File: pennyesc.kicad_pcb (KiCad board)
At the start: 2 copper layers, 34.5 x 40.2 mm, 52 parts, among them U1 MA782GGU-Z, U2 STM32L011F4Ux, U3 MP6536DU-LF-Z, U5 LM3480-3.3

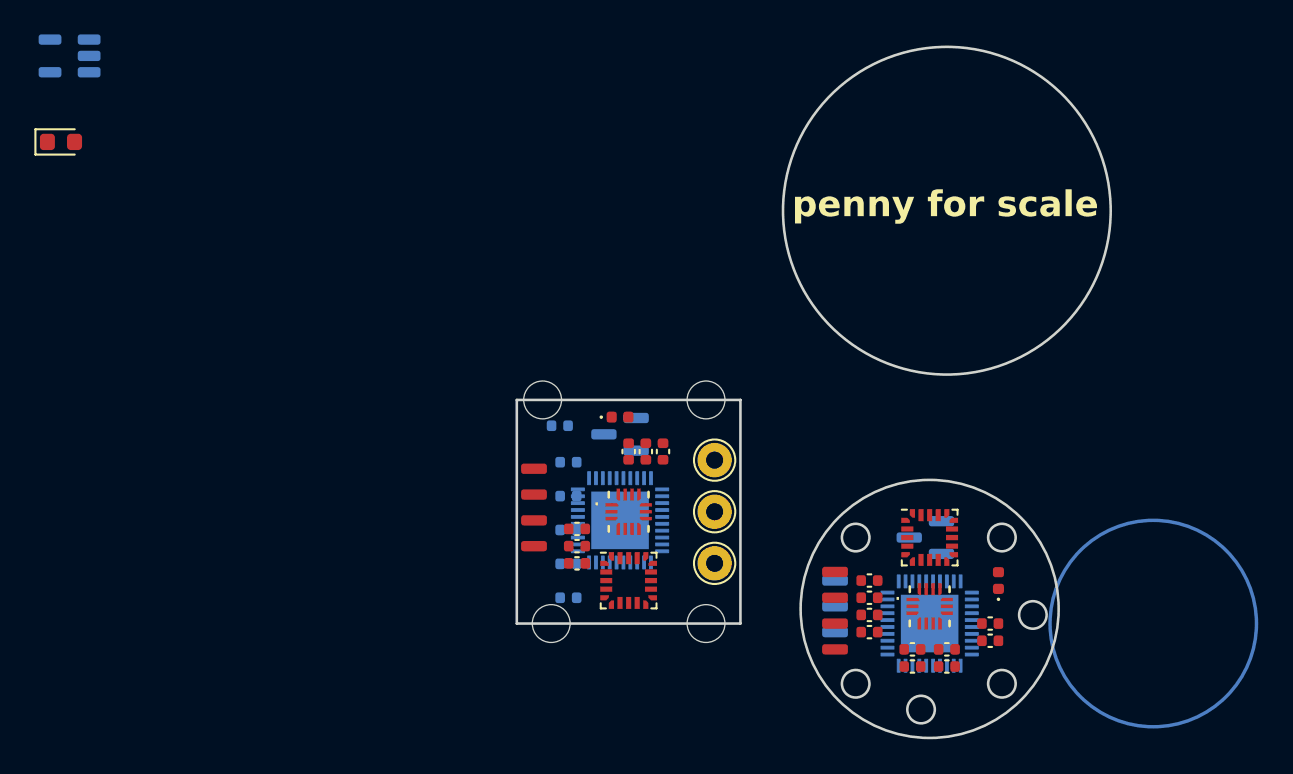
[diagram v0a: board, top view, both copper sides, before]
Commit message: pin assignment with stm32cube, pick LDO
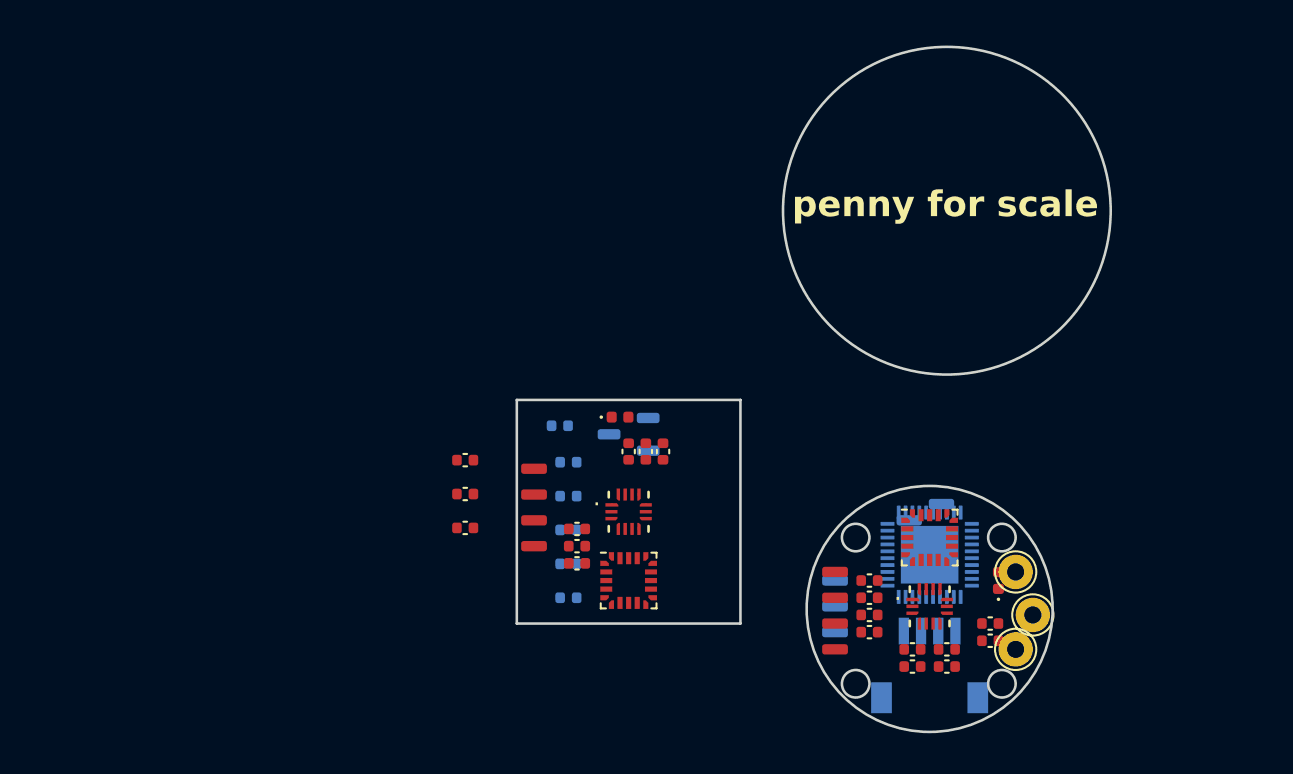
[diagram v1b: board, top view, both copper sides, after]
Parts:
- removed the REF** at (55.0, 47.0)
- removed the REF** at (45.5, 56.5)
- removed the REF** at (17.5, 23.5)
- removed the REF** at (55.0, 50.0)
- removed the REF** at (17.0, 28.5)
- removed the REF** at (55.0, 53.0)
- removed the REF** at (54.5, 56.5)
- removed the REF** at (54.5, 43.5)
- removed the REF** at (45.0, 43.5)
- removed the U3 at (67.5, 56.5)
- removed the U5 at (49.5, 45.5)
- added C10: 1uF, Capacitor_SMD:C_0402_1005Metric, F.Cu at (40.5, 50.9)
- added C7: 1uF, Capacitor_SMD:C_0402_1005Metric, F.Cu at (40.5, 47.0)
- added C9: 1uF, Capacitor_SMD:C_0402_1005Metric, F.Cu at (40.5, 49.0)
- added REF**: TestPoint_THTPad_D2.0mm_Drill1.0mm, TestPoint:TestPoint_THTPad_D2.0mm_Drill1.0mm, F.Cu at (73.5, 56.0)
- added REF**: JST_SM04B-SRSS-TB_LF__SN_, pennyesc:JST_SM04B-SRSS-TB(LF)(SN), B.Cu at (67.5, 56.9)
- added REF**: TestPoint_THTPad_D2.0mm_Drill1.0mm, TestPoint:TestPoint_THTPad_D2.0mm_Drill1.0mm, F.Cu at (72.5, 53.5)
- added REF**: TestPoint_THTPad_D2.0mm_Drill1.0mm, TestPoint:TestPoint_THTPad_D2.0mm_Drill1.0mm, F.Cu at (72.5, 58.0)
- added U6: XC6206P332MR-G, Package_TO_SOT_SMD:SOT-23-3, B.Cu at (50.0, 45.5)
- moved U3 18.1 mm to (67.5, 52.5)
- moved U5 1.00 mm to (67.2, 50.5)
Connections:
- net Net-(U5-VI) renamed VBUS
- U1 pad 1: unconnected-(U1-SCLK-Pad1) -> /SPI_SCLK
- U1 pad 11: unconnected-(U1-EN-Pad11) -> +3.3V
- U1 pad 5: unconnected-(U1-MISO-Pad5) -> /SPI_MISO
- U1 pad 6: unconnected-(U1-ASC-Pad6) -> GND
- U1 pad 8: unconnected-(U1-MOSI-Pad8) -> /SPI_MOSI
- U2 pad 10: unconnected-(U2-PA7-Pad10) -> /SPI_MOSI
- U2 pad 14: unconnected-(U2-PA9-Pad14) -> /UART_TX
- U2 pad 15: unconnected-(U2-PA10-Pad15) -> /UART_RX
- U2 pad 16: unconnected-(U2-PA13-Pad16) -> /SWDIO
- U2 pad 17: unconnected-(U2-PA14-Pad17) -> /SWCLK
- U2 pad 20: unconnected-(U2-PB9-Pad20) -> GND
- U2 pad 3: unconnected-(U2-NRST-Pad3) -> /NRST
- U2 pad 6: unconnected-(U2-PA1-Pad6) -> /UART_DE
- U2 pad 8: unconnected-(U2-PA5-Pad8) -> /SPI_SCLK
- U2 pad 9: unconnected-(U2-PA6-Pad9) -> /SPI_MISO
- U3 pad 12: unconnected-(U3-PWM1-Pad12) -> /PWM1
- U3 pad 13: unconnected-(U3-PWM2-Pad13) -> /PWM2
- U3 pad 15: unconnected-(U3-SHDNB-Pad15) -> +3.3V
- U3 pad 16: unconnected-(U3-PWM3-Pad16) -> /PWM3
- U3 pad 17: unconnected-(U3-STBYB-Pad17) -> /STBY
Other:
- board size 34.5 x 40.2 mm -> 34.5 x 39.8 mm

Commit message: switch to cheaper TI parts, passthrough shaft
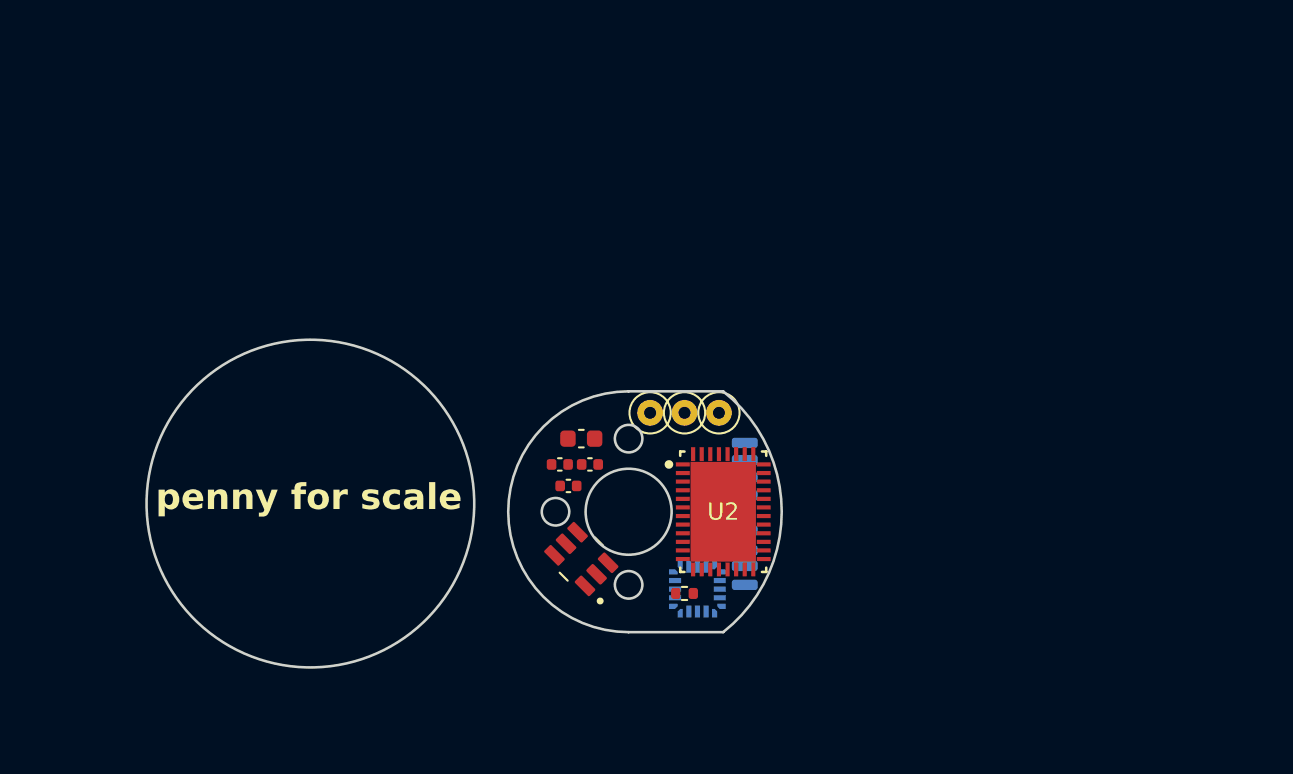
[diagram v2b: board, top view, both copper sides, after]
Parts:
- removed the C2 at (66.5, 58.0)
- removed the C2 at (71.0, 57.5)
- removed the C2 at (68.5, 58.0)
- removed the C2 at (64.0, 57.0)
- removed the C2 at (64.0, 56.0)
- removed the C2 at (68.5, 59.0)
- removed the C2 at (66.5, 59.0)
- removed the C2 at (47.0, 53.0)
- removed the C2 at (46.5, 47.1)
- removed the C2 at (50.0, 46.5)
- removed the C2 at (52.0, 46.5)
- removed the C2 at (64.0, 55.0)
- removed the C2 at (51.0, 46.5)
- removed the C2 at (64.0, 54.0)
- removed the C2 at (71.0, 56.5)
- removed the C2 at (47.0, 51.0)
- removed the C2 at (47.0, 52.0)
- removed C4: 0.1uF, Capacitor_SMD:C_0402_1005Metric
- removed the REF** at (49.5, 44.5)
- removed the REF** at (44.5, 47.5)
- removed the REF** at (62.0, 53.5)
- removed the REF** at (73.5, 56.0)
- removed the REF** at (44.5, 49.0)
- removed the REF** at (67.5, 56.9)
- removed the REF** at (62.0, 54.0)
- removed the REF** at (62.0, 57.0)
- removed the REF** at (62.0, 55.5)
- removed the REF** at (72.5, 58.0)
- removed the REF** at (62.0, 55.0)
- removed the REF** at (62.0, 56.5)
- removed the REF** at (62.0, 58.0)
- removed the REF** at (44.5, 52.0)
- removed the REF** at (44.5, 50.5)
- removed the REF** at (71.5, 54.0)
- removed the U1 at (50.0, 50.0)
- removed the U1 at (67.5, 55.5)
- removed the U2 at (67.5, 51.5)
- removed the U2 at (50.0, 54.0)
- removed U5: LM3480-3.3, Package_TO_SOT_SMD:SOT-23
- removed U6: XC6206P332MR-G, Package_TO_SOT_SMD:SOT-23-3
- added R1: 22R, Resistor_SMD:R_0402_1005Metric, F.Cu at (53.2, 54.8)
- added REF**: TestPoint_THTPad_D2.0mm_Drill1.0mm, TestPoint:TestPoint_THTPad_D2.0mm_Drill1.0mm, F.Cu at (53.2, 44.2)
- added REF**: TestPoint_THTPad_D2.0mm_Drill1.0mm, TestPoint:TestPoint_THTPad_D2.0mm_Drill1.0mm, F.Cu at (51.2, 44.2)
- added TP1: TestPoint, pennyesc:TestPoint_Pad_Rect, B.Cu at (56.8, 48.0)
- added TP2: TestPoint, pennyesc:TestPoint_Pad_Rect, B.Cu at (56.8, 46.0)
- added TP3: TestPoint, pennyesc:TestPoint_Pad_Rect, B.Cu at (56.8, 47.0)
- added TP4: TestPoint, pennyesc:TestPoint_Pad_Rect, B.Cu at (56.8, 49.0)
- added TP5: TestPoint, pennyesc:TestPoint_Pad_Rect, B.Cu at (56.8, 51.1)
- added TP6: TestPoint, pennyesc:TestPoint_Pad_Rect, B.Cu at (56.8, 53.1)
- added TP7: TestPoint, pennyesc:TestPoint_Pad_Rect, B.Cu at (56.8, 54.2)
- added TP8: TestPoint, pennyesc:TestPoint_Pad_Rect, B.Cu at (56.8, 52.2)
- added U1: STM32L011F4Ux, Package_DFN_QFN:ST_UFQFPN-20_3x3mm_P0.5mm, B.Cu at (54.0, 54.5)
- added U2: MCT8316Z0RRGFR, pennyesc:MCT8316Z0RRGFR-IPC_C, F.Cu at (55.5, 50.0)
- C3: value 0.1uF -> 22uF; footprint Capacitor_SMD:C_0402_1005Metric -> Capacitor_SMD:C_0603_1608Metric; moved to F.Cu
- U3: value MP6536DU-LF-Z -> TMAG5273A1QDBVR; footprint pennyesc:QFN40P500X500X100-41N_MP6536DU-LF-Z -> pennyesc:SOT95P280X140-6N; moved to F.Cu
- moved U3 20.3 mm to (47.2, 52.8), turned to 135 degrees
- moved REF** 19.6 mm to (55.2, 44.2)
- moved C1 9.50 mm to (54.5, 49.2)
- moved C5 9.45 mm to (54.5, 48.0)
- moved C6 9.18 mm to (54.5, 50.5)
- moved C7 7.25 mm to (47.8, 47.2)
- moved C1 6.48 mm to (46.5, 48.5)
- moved C2 5.76 mm to (46.0, 47.2)
- moved C3 3.42 mm to (47.2, 45.8), turned to 0 degrees
- renumbered C10 to C1, C9 to C2
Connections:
- C3 pad 1: Net-(U3-BST2) -> GND
- C3 pad 2: Net-(C3-Pad2) -> Net-(U2-FB_BK)
- U3 pad 1: Net-(C3-Pad2) -> /I2C_SCL
- U3 pad 2: Net-(C3-Pad2) -> GND
- U3 pad 3: VBUS -> GND
- U3 pad 4: VBUS -> +3.3V
- U3 pad 5: VBUS -> unconnected-(U3-~{INT}-Pad5)
- U3 pad 6: Net-(C4-Pad2) -> /I2C_SDA
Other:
- board size 34.5 x 39.8 mm -> 36.9 x 19 mm

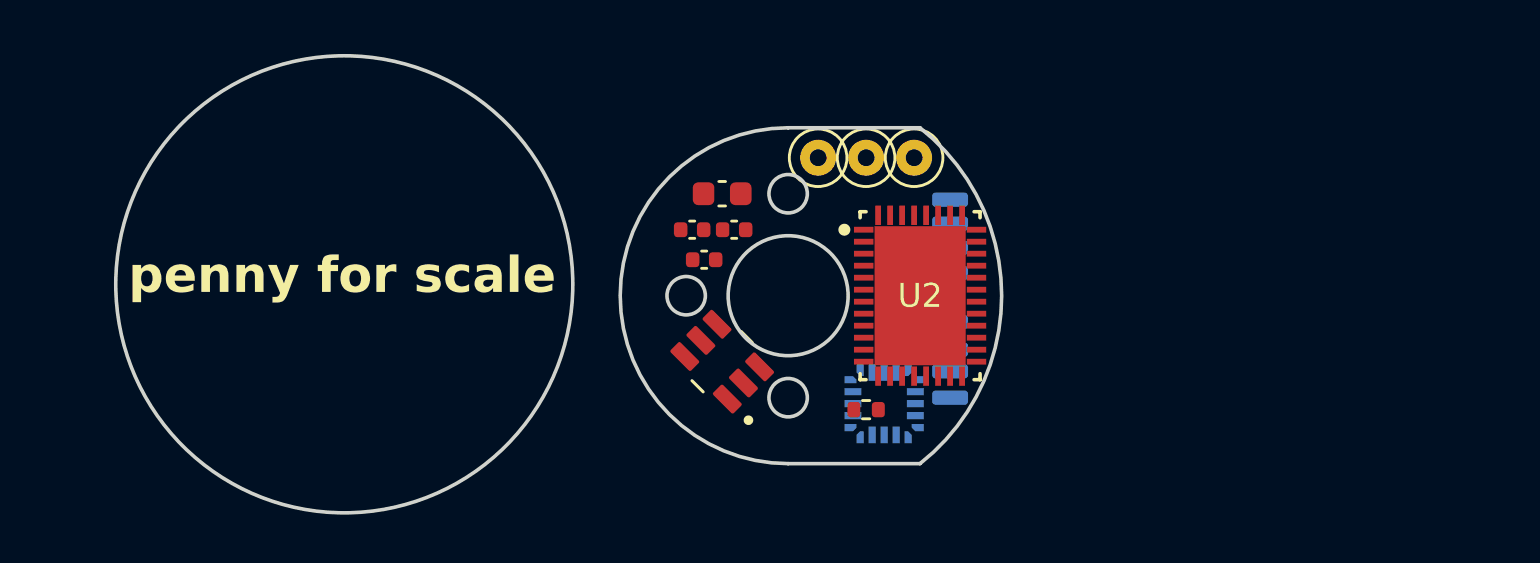
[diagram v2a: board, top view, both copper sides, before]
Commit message: chose R and C values, set jlcpcb constraints, started layout
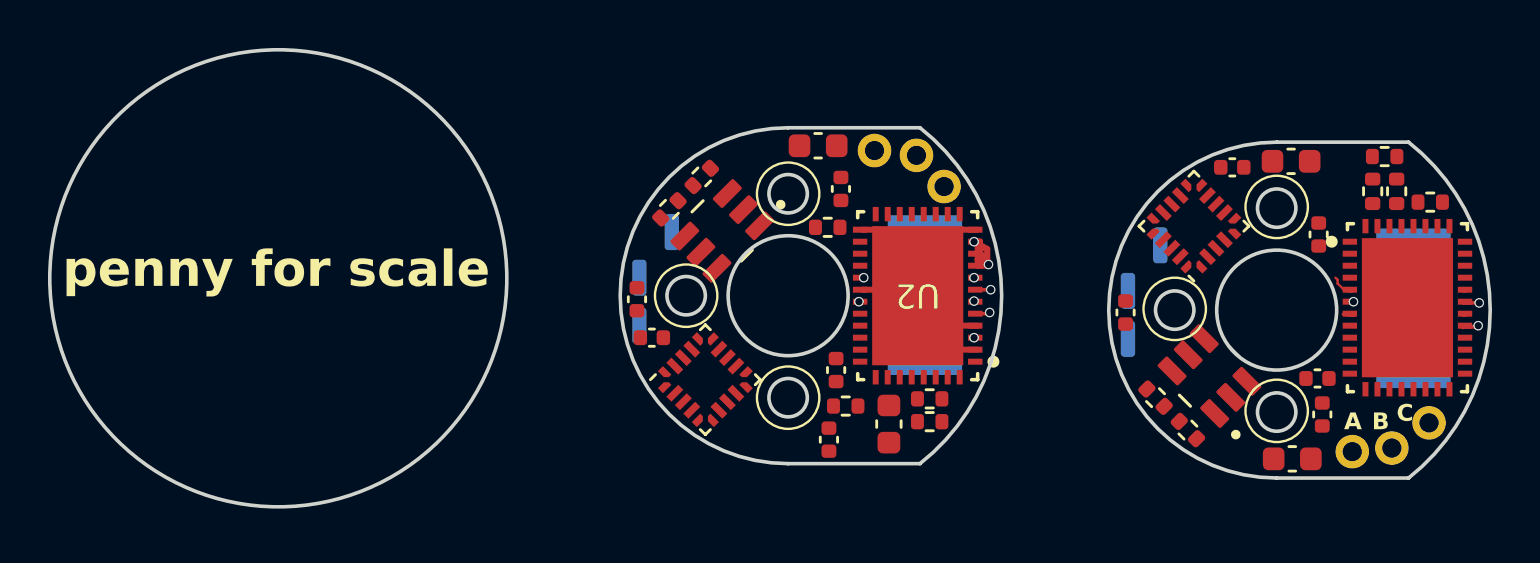
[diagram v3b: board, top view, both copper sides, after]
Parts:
- removed the C5 at (54.5, 48.0)
- removed the C6 at (54.5, 50.5)
- removed the C7 at (47.8, 47.2)
- removed REF** (x3): TestPoint_THTPad_D2.0mm_Drill1.0mm, TestPoint:TestPoint_THTPad_D2.0mm_Drill1.0mm
- added C2: 1uF, Capacitor_SMD:C_0402_1005Metric, F.Cu at (68.5, 44.6)
- added C3: 22uF, Capacitor_SMD:C_0603_1608Metric, F.Cu at (71.0, 44.4)
- added C4: 0.1uF, Capacitor_SMD:C_0402_1005Metric, F.Cu at (52.0, 53.1)
- added C4: 0.1uF, Capacitor_SMD:C_0402_1005Metric, F.Cu at (72.1, 47.5)
- added C5: 1uF, Capacitor_SMD:C_0402_1005Metric, F.Cu at (51.7, 56.0)
- added C5: 1uF, Capacitor_SMD:C_0402_1005Metric, F.Cu at (72.1, 53.5)
- added C6: 0.1uF, Capacitor_SMD:C_0402_1005Metric, F.Cu at (52.2, 45.5)
- added C6: 0.1uF, Capacitor_SMD:C_0402_1005Metric, F.Cu at (72.3, 55.0)
- added C7: 10uF, Capacitor_SMD:C_0603_1608Metric, F.Cu at (51.2, 43.8)
- added C7: 10uF, Capacitor_SMD:C_0603_1608Metric, F.Cu at (71.0, 56.8)
- added R1: 22R, Resistor_SMD:R_0402_1005Metric, F.Cu at (74.4, 45.6)
- added R2: 3.3k, Resistor_SMD:R_0402_1005Metric, F.Cu at (76.8, 46.1)
- added R2: 3.3k, Resistor_SMD:R_0402_1005Metric, F.Cu at (51.6, 47.1)
- added R3: 3.3k, Resistor_SMD:R_0402_1005Metric, F.Cu at (75.4, 45.6)
- added R3: 3.3k, Resistor_SMD:R_0402_1005Metric, F.Cu at (55.9, 54.3)
- added R4: 2k, Resistor_SMD:R_0402_1005Metric, F.Cu at (74.9, 44.2)
- added R4: 2k, Resistor_SMD:R_0402_1005Metric, F.Cu at (55.9, 55.2)
- added R5: 3.3k, Resistor_SMD:R_0402_1005Metric, F.Cu at (45.0, 46.4)
- added R5: 3.3k, Resistor_SMD:R_0402_1005Metric, F.Cu at (66.7, 55.6)
- added R6: 3.3k, Resistor_SMD:R_0402_1005Metric, F.Cu at (65.3, 54.2)
- added R6: 3.3k, Resistor_SMD:R_0402_1005Metric, F.Cu at (46.4, 45.0)
- added TP1: TestPoint, pennyesc:TestPoint_Pad_Rect, B.Cu at (65.5, 47.9)
- added TP2: TestPoint, pennyesc:TestPoint_Pad_Rect, B.Cu at (76.9, 51.1)
- added TP3: TestPoint, pennyesc:TestPoint_Pad_Rect, B.Cu at (76.9, 50.0)
- added TP4: TestPoint, pennyesc:TestPoint_Pad_Rect, B.Cu at (64.2, 51.8)
- added TP5: TestPoint, pennyesc:TestPoint_Pad_Rect, B.Cu at (64.2, 49.8)
- added TP6: TestPoint, pennyesc:SolderHole_1.0x1.6mm, B.Cu at (73.5, 56.5)
- added TP7: TestPoint, pennyesc:SolderHole_1.0x1.6mm, B.Cu at (75.2, 56.4)
- added TP8: TestPoint, pennyesc:SolderHole_1.0x1.6mm, B.Cu at (76.7, 55.3)
- added U1: STM32L011F4Ux, Package_DFN_QFN:ST_UFQFPN-20_3x3mm_P0.5mm, F.Cu at (66.9, 47.1)
- added U2: MCT8316Z0RRGFR, pennyesc:MCT8316Z0RRGFR-IPC_C, F.Cu at (75.8, 50.5)
- added U3: TMAG5273A1QDBVR, pennyesc:SOT95P280X140-6N, F.Cu at (67.6, 53.4)
- C1: value C_Small -> 1uF; moved to F.Cu
- TP6, TP7, TP8: footprint pennyesc:TestPoint_Pad_Rect -> pennyesc:SolderHole_1.0x1.6mm
- U1: moved to F.Cu
- moved TP4 13.1 mm to (43.8, 51.2), turned to 180 degrees
- moved TP5 13.1 mm to (43.8, 49.2), turned to 180 degrees
- moved C3 11.9 mm to (54.2, 55.4), turned to 90 degrees
- moved TP1 11.6 mm to (45.1, 47.4), turned to 180 degrees
- moved TP7 10.2 mm to (55.4, 44.1)
- moved C1 9.67 mm to (64.1, 50.7), turned to 90 degrees
- moved TP8 8.88 mm to (53.6, 44.0)
- moved TP6 7.70 mm to (56.5, 45.5)
- moved U1 7.52 mm to (46.5, 53.5), turned to 45 degrees
- moved U3 5.45 mm to (47.2, 47.3), turned to -135 degrees
- moved C2 4.80 mm to (44.3, 51.8)
- moved TP2 4.56 mm to (56.5, 50.5), turned to 90 degrees
- moved C1 3.25 mm to (43.7, 50.1), turned to 90 degrees
- moved TP3 2.41 mm to (56.5, 49.4), turned to 90 degrees
- moved R1 0.86 mm to (52.4, 54.6)
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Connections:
- C1 pad 1: VBUS -> +3.3V
- U2 pad 37: unconnected-(U2-ILIM-Pad37) -> Net-(U2-ILIM)
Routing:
- net VBUS: track 0.00 -> 4.39 mm, vias 0 -> 2
- net GND: track 0.00 -> 3.41 mm
- net Net-(U2-SW_BK): track 0.00 -> 1.73 mm, vias 0 -> 1
- net Net-(U2-CPH): track 0.00 -> 1.45 mm, vias 0 -> 1
- net /HALLA: track 0.00 -> 1.10 mm, vias 0 -> 2
- net +3.3V: track 0.00 -> 0.83 mm, vias 0 -> 2
- net Net-(U2-CPL): track 0.00 -> 0.31 mm, vias 0 -> 2
- net Net-(U2-CP): track 0.00 -> 0.15 mm, vias 0 -> 1
- net Net-(U2-FB_BK): vias 0 -> 1
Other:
- board size 36.9 x 19 mm -> 60 x 19 mm
- copper layers 2 -> 4
- board text added: "A"
- board text added: "B"
- board text added: "C"
